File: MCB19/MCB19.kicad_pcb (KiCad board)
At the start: 2 copper layers, 94 parts, among them J401 USART, J402 DISABLE, J601 RJ45, J602 RJ45, J611 +BATT, J612 GND, J613 VBAT+, J614 VBAT-, Q601 IRFP260N, Q602 IRFP260N, U201 MCP2551-I/SN, U202 MCP2515-xSO, U301 LM7805, U401 ATMEGA328P-PU, U501 LM7815, U601 LM5104MNOPB, U602 INA211_DCK_6, U603 LM324, Y201 16MHz, Y401 16MHz

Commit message: Versão 2.1
Tinha uma trilha com problema
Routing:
- net GND: track 203.9 -> 206.9 mm
- net (no net): track 7.95 -> 4.95 mm
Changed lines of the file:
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@@
   (segment (start 125.5 69.5) (end 125.5 71.4) (width 0.508) (layer B.Cu) (net 1))
   (via (at 125.5 69.5) (size 1.5) (drill 0.8) (layers F.Cu B.Cu) (net 1))
+  (via (at 59 136.5) (size 1.5) (drill 0.8) (layers F.Cu B.Cu) (net 1))
+  (via (at 60 124) (size 1.5) (drill 0.8) (layers F.Cu B.Cu) (net 1))
+  (via (at 63.5 127.5) (size 1.5) (drill 0.8) (layers F.Cu B.Cu) (net 1))
   (segment (start 78.329 155.146) (end 79.759 155.146) (width 0.762) (layer B.Cu) (net 2))
   (segment (start 80.394 155.146) (end 79.759 155.146) (width 0.762) (layer B.Cu) (net 2))
@@
   (segment (start 120.55 73.45) (end 119.5 74.5) (width 0.508) (layer B.Cu) (net 36))
   (segment (start 119.5 74.5) (end 119.5 75.9875) (width 0.508) (layer B.Cu) (net 36))
+  (via (at 122 78) (size 1.5) (drill 0.8) (layers F.Cu B.Cu) (net 36))
   (segment (start 54 105.5) (end 56.625 105.5) (width 0.762) (layer B.Cu) (net 37))
   (segment (start 56.71 105.585) (end 56.625 105.5) (width 0.762) (layer B.Cu) (net 37))
@@
   (segment (start 71.125 126.975) (end 71.41 126.69) (width 0.762) (layer B.Cu) (net 38))
   (via (at 123 69.5) (size 1.5) (drill 0.8) (layers F.Cu B.Cu) (net 39))
+  (segment (start 64.5 103.45) (end 66.55 103.45) (width 0.508) (layer B.Cu) (net 39))
+  (segment (start 66.55 103.45) (end 66.55 103.45) (width 0.508) (layer B.Cu) (net 39))
+  (via (at 66.55 103.45) (size 1.5) (drill 0.8) (layers F.Cu B.Cu) (net 39))
   (segment (start 77.03 119.07) (end 76.95 119.15) (width 0.762) (layer B.Cu) (net 40))
   (segment (start 77.03 116.15) (end 77.03 119.07) (width 0.762) (layer B.Cu) (net 40))
@@
   (segment (start 103 84.475) (end 102.975 84.5) (width 0.762) (layer F.Cu) (net 46))
   (segment (start 103 82) (end 103 84.475) (width 0.762) (layer F.Cu) (net 46))
+  (via (at 84.5 103) (size 1.5) (drill 0.8) (layers F.Cu B.Cu) (net 46))
+  (via (at 88 96.5) (size 1.5) (drill 0.8) (layers F.Cu B.Cu) (net 46))
+  (segment (start 84.985 96.5) (end 88 96.5) (width 0.635) (layer F.Cu) (net 46))
+  (segment (start 84.5 103) (end 87.025 103) (width 0.635) (layer F.Cu) (net 46))
+  (segment (start 87.025 102.77) (end 87.025 103) (width 0.508) (layer F.Cu) (net 46))
+  (segment (start 87.025 103) (end 87.025 104.925) (width 0.508) (layer F.Cu) (net 46))
+  (segment (start 88 96.5) (end 88 94) (width 0.635) (layer B.Cu) (net 46))
+  (segment (start 82.626 94) (end 88 94) (width 1.524) (layer B.Cu) (net 46))
+  (segment (start 88 94) (end 101.724 94) (width 1.524) (layer B.Cu) (net 46))
+  (segment (start 85.56066 103) (end 84.5 103) (width 0.635) (layer B.Cu) (net 46))
+  (segment (start 95.171902 103) (end 85.56066 103) (width 0.635) (layer B.Cu) (net 46))
+  (segment (start 95.967501 102.204401) (end 95.171902 103) (width 0.635) (layer B.Cu) (net 46))
+  (segment (start 95.967501 97.467501) (end 95.967501 102.204401) (width 0.635) (layer B.Cu) (net 46))
+  (segment (start 88 96.5) (end 95 96.5) (width 0.635) (layer B.Cu) (net 46))
+  (segment (start 95 96.5) (end 95.967501 97.467501) (width 0.635) (layer B.Cu) (net 46))
   (segment (start 76 88.95) (end 75.95 89) (width 0.762) (layer F.Cu) (net 47))
   (segment (start 76 84.5) (end 76 88.95) (width 0.762) (layer F.Cu) (net 47))
@@
   (segment (start 93 109) (end 93 109.5) (width 0.508) (layer F.Cu) (net 48))
   (segment (start 89 105) (end 93 109) (width 0.508) (layer F.Cu) (net 48))
+  (via (at 128 69.5) (size 1.5) (drill 0.8) (layers F.Cu B.Cu) (net 49))
+  (segment (start 128.525 68.975) (end 128 69.5) (width 0.508) (layer B.Cu) (net 49))
+  (segment (start 128.525 67.81) (end 128.525 68.975) (width 0.508) (layer B.Cu) (net 49))
+  (segment (start 54 103.45) (end 51.95 103.45) (width 0.508) (layer B.Cu) (net 49))
+  (segment (start 51.95 103.45) (end 51.95 103.45) (width 0.508) (layer B.Cu) (net 49))
+  (via (at 51.95 103.45) (size 1.5) (drill 0.8) (layers F.Cu B.Cu) (net 49))
+  (segment (start 128.525 61.46) (end 128.525 62.73) (width 0.508) (layer B.Cu) (net 50))
+  (segment (start 133.475 61.46) (end 133.475 62.73) (width 0.508) (layer B.Cu) (net 51))
+  (segment (start 133.475 65.27) (end 133.475 66.54) (width 0.508) (layer B.Cu) (net 52))
   (segment (start 76.064 175.458) (end 74.794 174.188) (width 0.762) (layer B.Cu) (net 59))
   (segment (start 76.064 176.728) (end 76.064 175.458) (width 0.762) (layer B.Cu) (net 59))
@@
   (segment (start 48.4 101.5) (end 52.5 101.5) (width 0.508) (layer B.Cu) (net 62))
   (segment (start 66 101.5) (end 67.5 101.5) (width 0.508) (layer B.Cu) (net 62))
+  (segment (start 66 101.5) (end 61.5 101.5) (width 0.508) (layer B.Cu) (net 62))
+  (segment (start 57 101.5) (end 52.5 101.5) (width 0.508) (layer B.Cu) (net 62))
+  (via (at 57 101.5) (size 1.5) (drill 0.8) (layers F.Cu B.Cu) (net 62))
+  (via (at 61.5 101.5) (size 1.5) (drill 0.8) (layers F.Cu B.Cu) (net 62))
+  (segment (start 57 101.5) (end 61.5 101.5) (width 0.508) (layer F.Cu) (net 62))
   (segment (start 78.05 84.5) (end 80 84.5) (width 0.762) (layer F.Cu) (net 63))
   (segment (start 80 83.5) (end 80 84.5) (width 0.762) (layer F.Cu) (net 63))
@@
   (segment (start 96.492956 109.4) (end 108.2 109.4) (width 0.508) (layer F.Cu) (net 68))
   (segment (start 108.2 109.4) (end 109.5 110.7) (width 0.508) (layer F.Cu) (net 68))
+  (segment (start 97.45 106) (end 99.95 103.5) (width 0.508) (layer F.Cu) (net 68))
+  (segment (start 97.45 106.5) (end 97.45 106) (width 0.508) (layer F.Cu) (net 68))
   (segment (start 56.025 168.425) (end 56.1 168.5) (width 0.762) (layer B.Cu) (net 69))
   (segment (start 56.025 164.5) (end 56.025 168.425) (width 0.762) (layer B.Cu) (net 69))
@@
   (segment (start 62.5 160) (end 62.5 162.75) (width 0.762) (layer B.Cu) (net 69))
   (segment (start 61.954 159.454) (end 62.5 160) (width 0.762) (layer B.Cu) (net 69))
-  (segment (start 97.45 106) (end 99.95 103.5) (width 0.508) (layer F.Cu) (net 68))
-  (segment (start 97.45 106.5) (end 97.45 106) (width 0.508) (layer F.Cu) (net 68))
-  (via (at 84.5 103) (size 1.5) (drill 0.8) (layers F.Cu B.Cu) (net 46))
-  (via (at 88 96.5) (size 1.5) (drill 0.8) (layers F.Cu B.Cu) (net 46))
-  (segment (start 84.985 96.5) (end 88 96.5) (width 0.635) (layer F.Cu) (net 46))
-  (segment (start 84.5 103) (end 87.025 103) (width 0.635) (layer F.Cu) (net 46))
-  (segment (start 87.025 102.77) (end 87.025 103) (width 0.508) (layer F.Cu) (net 46))
-  (segment (start 87.025 103) (end 87.025 104.925) (width 0.508) (layer F.Cu) (net 46))
-  (segment (start 88 96.5) (end 88 94) (width 0.635) (layer B.Cu) (net 46))
-  (segment (start 82.626 94) (end 88 94) (width 1.524) (layer B.Cu) (net 46))
-  (segment (start 88 94) (end 101.724 94) (width 1.524) (layer B.Cu) (net 46))
-  (segment (start 85.56066 103) (end 84.5 103) (width 0.635) (layer B.Cu) (net 46))
-  (segment (start 95.171902 103) (end 85.56066 103) (width 0.635) (layer B.Cu) (net 46))
-  (segment (start 95.967501 102.204401) (end 95.171902 103) (width 0.635) (layer B.Cu) (net 46))
-  (segment (start 95.967501 97.467501) (end 95.967501 102.204401) (width 0.635) (layer B.Cu) (net 46))
-  (segment (start 88 96.5) (end 95 96.5) (width 0.635) (layer B.Cu) (net 46))
-  (segment (start 95 96.5) (end 95.967501 97.467501) (width 0.635) (layer B.Cu) (net 46))
-  (segment (start 128.525 61.46) (end 128.525 62.73) (width 0.508) (layer B.Cu) (net 50))
-  (segment (start 133.475 61.46) (end 133.475 62.73) (width 0.508) (layer B.Cu) (net 51))
-  (segment (start 133.475 65.27) (end 133.475 66.54) (width 0.508) (layer B.Cu) (net 52))
-  (via (at 128 69.5) (size 1.5) (drill 0.8) (layers F.Cu B.Cu) (net 49))
-  (segment (start 128.525 68.975) (end 128 69.5) (width 0.508) (layer B.Cu) (net 49))
-  (segment (start 128.525 67.81) (end 128.525 68.975) (width 0.508) (layer B.Cu) (net 49))
-  (via (at 122 78) (size 1.5) (drill 0.8) (layers F.Cu B.Cu) (net 36))
-  (segment (start 64.5 103.45) (end 66.55 103.45) (width 0.508) (layer B.Cu) (net 39))
-  (segment (start 66.55 103.45) (end 66.55 103.45) (width 0.508) (layer B.Cu) (net 39))
-  (via (at 66.55 103.45) (size 1.5) (drill 0.8) (layers F.Cu B.Cu) (net 39))
-  (segment (start 54 103.45) (end 51.95 103.45) (width 0.508) (layer B.Cu) (net 49))
-  (segment (start 51.95 103.45) (end 51.95 103.45) (width 0.508) (layer B.Cu) (net 49))
-  (via (at 51.95 103.45) (size 1.5) (drill 0.8) (layers F.Cu B.Cu) (net 49))
-  (segment (start 66 101.5) (end 61.5 101.5) (width 0.508) (layer B.Cu) (net 62))
-  (segment (start 57 101.5) (end 52.5 101.5) (width 0.508) (layer B.Cu) (net 62))
-  (via (at 57 101.5) (size 1.5) (drill 0.8) (layers F.Cu B.Cu) (net 62))
-  (via (at 61.5 101.5) (size 1.5) (drill 0.8) (layers F.Cu B.Cu) (net 62))
-  (segment (start 57 101.5) (end 61.5 101.5) (width 0.508) (layer F.Cu) (net 62))
-  (via (at 59 136.5) (size 1.5) (drill 0.8) (layers F.Cu B.Cu) (net 1))
-  (via (at 60 124) (size 1.5) (drill 0.8) (layers F.Cu B.Cu) (net 1))
-  (via (at 63.5 127.5) (size 1.5) (drill 0.8) (layers F.Cu B.Cu) (net 1))
   (segment (start 60 124) (end 63.5 127.5) (width 0.762) (layer F.Cu) (net 0))
-  (segment (start 59 133.5) (end 59 136.5) (width 0.762) (layer F.Cu) (net 0))
-  (via (at 92.5 129) (size 1.5) (drill 0.8) (layers F.Cu B.Cu) (net 39))
+  (segment (start 59 133.5) (end 59 136.5) (width 0.762) (layer F.Cu) (net 1))
   (via (at 59 133.5) (size 1.5) (drill 0.8) (layers F.Cu B.Cu) (net 1))
   (via (at 66.04 40.64) (size 1.5) (drill 0.8) (layers F.Cu B.Cu) (net 1))
@@
   (segment (start 62.5 139) (end 68.046 133.454) (width 0.762) (layer F.Cu) (net 32))
   (segment (start 68.046 133.454) (end 99.96 133.454) (width 0.762) (layer F.Cu) (net 32))
+  (via (at 92.5 129) (size 1.5) (drill 0.8) (layers F.Cu B.Cu) (net 39))
   (segment (start 63 130.5) (end 75.10812 130.5) (width 0.762) (layer F.Cu) (net 39))
   (segment (start 58.5 126) (end 63 130.5) (width 0.762) (layer F.Cu) (net 39))

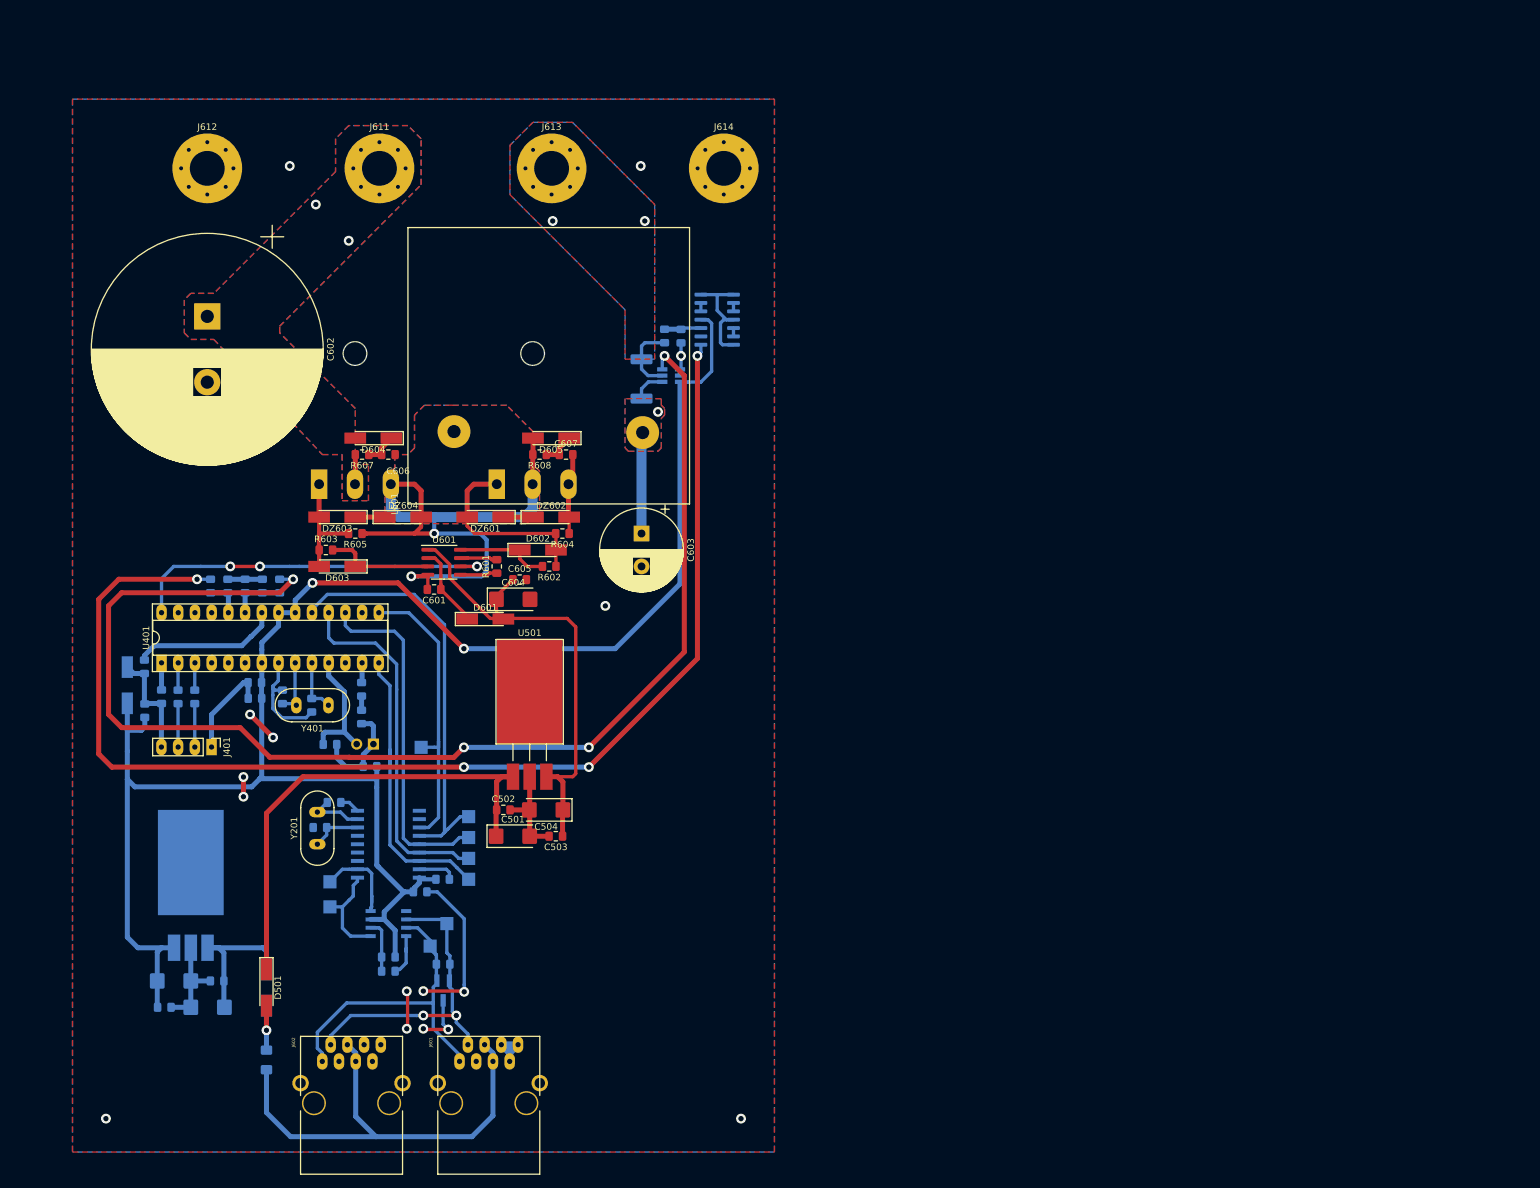
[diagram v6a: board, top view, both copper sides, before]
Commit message: Versão 2.2
Funcional, com a centralização dos mosfets, e a aplicação de um DRC para garantia de funcionamento
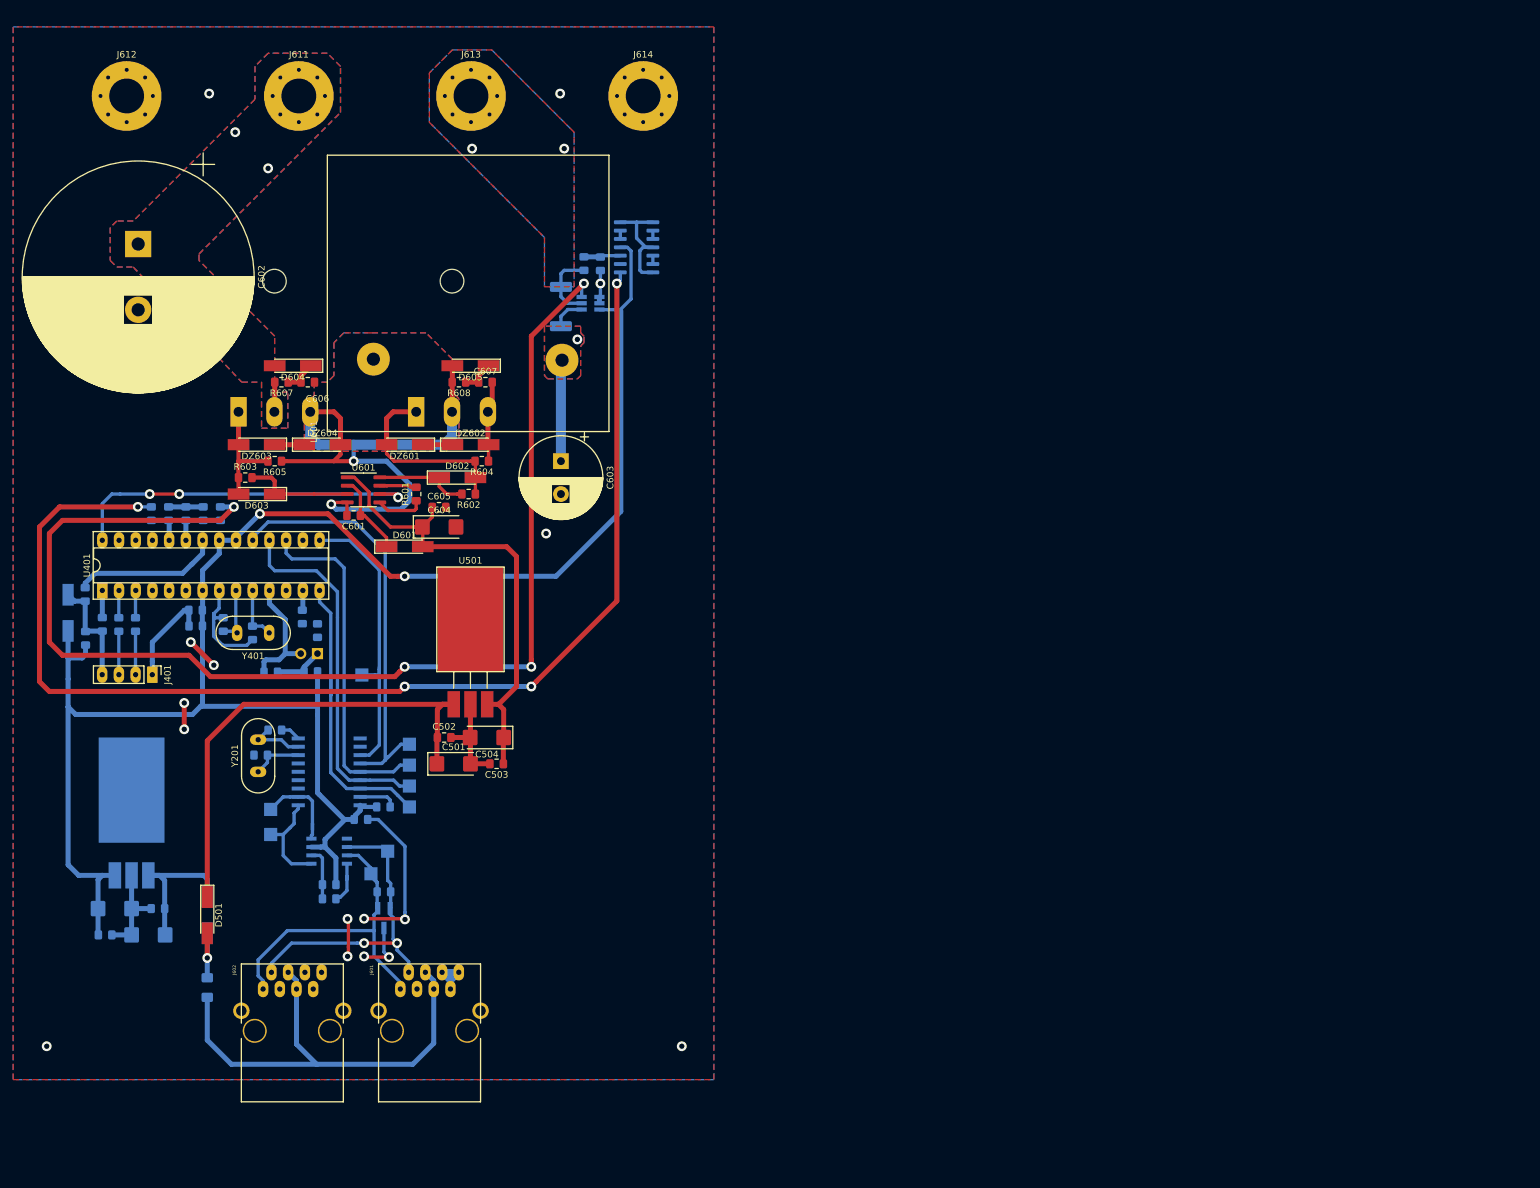
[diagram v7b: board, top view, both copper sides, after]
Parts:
- moved C201 17.0 mm to (69.2, 117.5)
- moved C601 16.6 mm to (75.8, 93.8)
- moved R603 16.5 mm to (59.3, 88.0)
- moved C603 16.5 mm to (107.2, 85.5)
- moved C605 16.5 mm to (88.7, 92.5)
- moved C606 16.5 mm to (68.8, 73.5)
- moved C607 16.5 mm to (95.8, 73.5)
- moved D601 16.5 mm to (83.5, 98.5)
- moved D602 16.5 mm to (91.5, 88.0)
- moved D603 16.5 mm to (61.0, 90.5)
- moved D604 16.5 mm to (66.5, 71.0)
- moved D605 16.5 mm to (93.5, 71.0)
- moved DZ601 16.5 mm to (83.5, 83.0)
- moved DZ602 16.5 mm to (93.5, 83.0)
- moved DZ603 16.5 mm to (61.0, 83.0)
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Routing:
- net /MCU/INALLL: track 193.6 -> 188.1 mm
- net (no net): track 4.95 -> 0.00 mm
- net /driver/LM324A: track 188.3 -> 186.0 mm
- net Net-(D403-Pad2): track 2.15 -> 0.00 mm
- net +5V: track 281.1 -> 283.3 mm
- net +15V: track 74.1 -> 72.0 mm
- net /MCU/PWM: track 56.4 -> 54.6 mm
- net GND: track 206.9 -> 205.2 mm
- net Net-(R601-Pad1): track 5.65 -> 7.36 mm
- net Net-(J402-Pad2): track 19.1 -> 18.3 mm
